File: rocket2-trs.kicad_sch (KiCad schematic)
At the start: 25 parts, among them J2 ARM Cortex Debug, J2 SMA, U4 AZ1117-3.3, Y1 16MHz

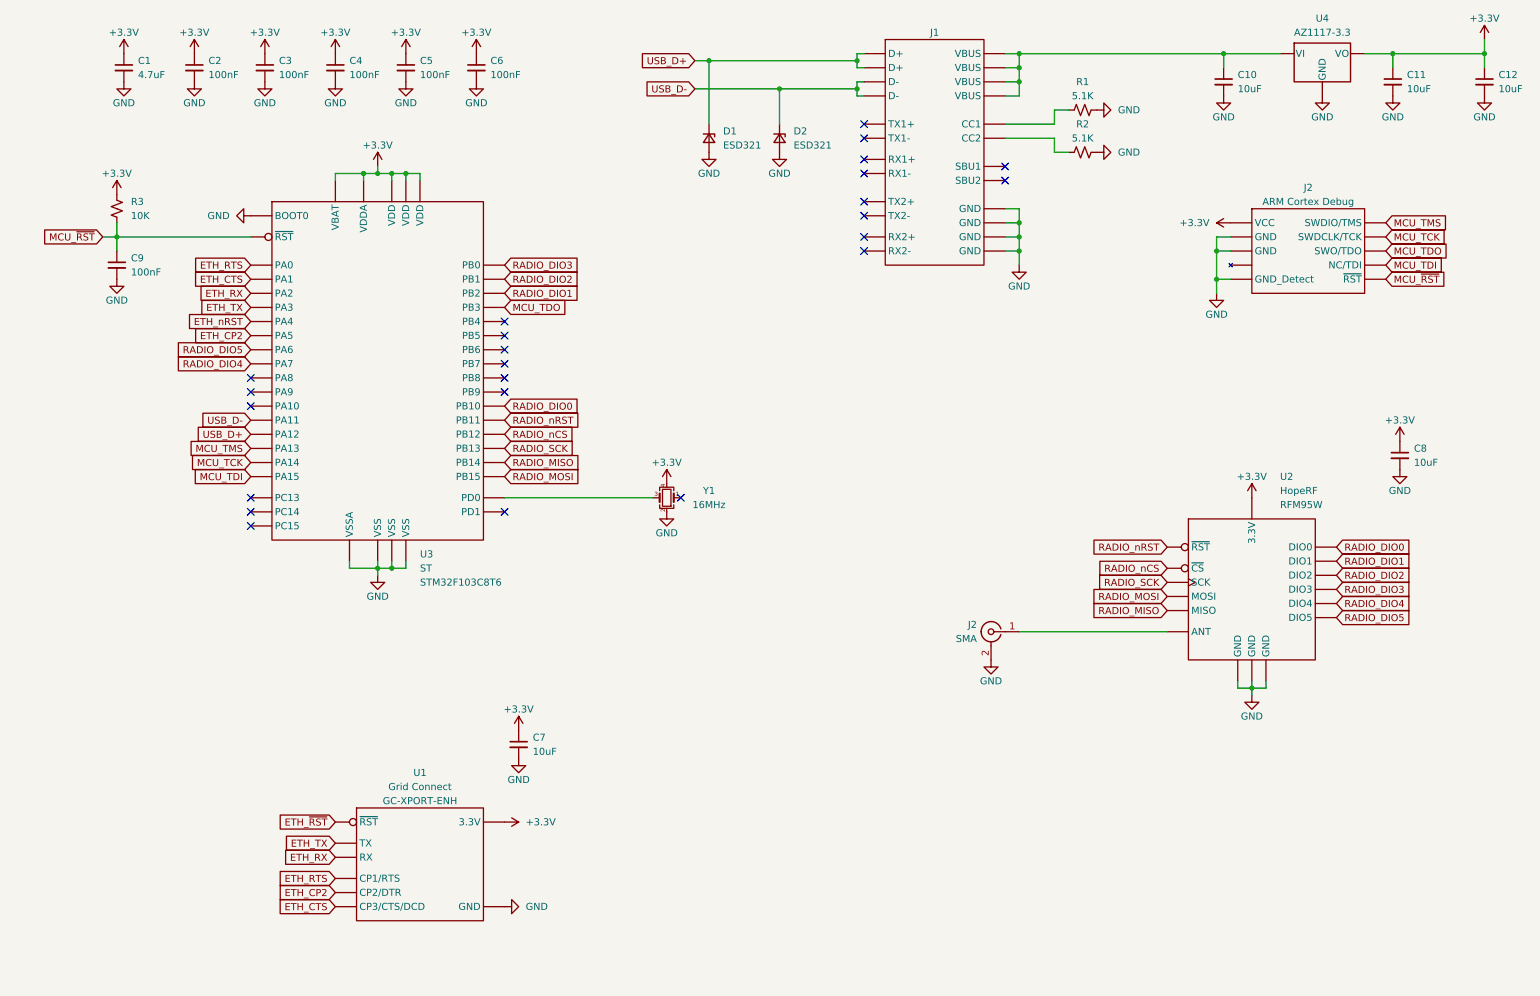
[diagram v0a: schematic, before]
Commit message: Add test points
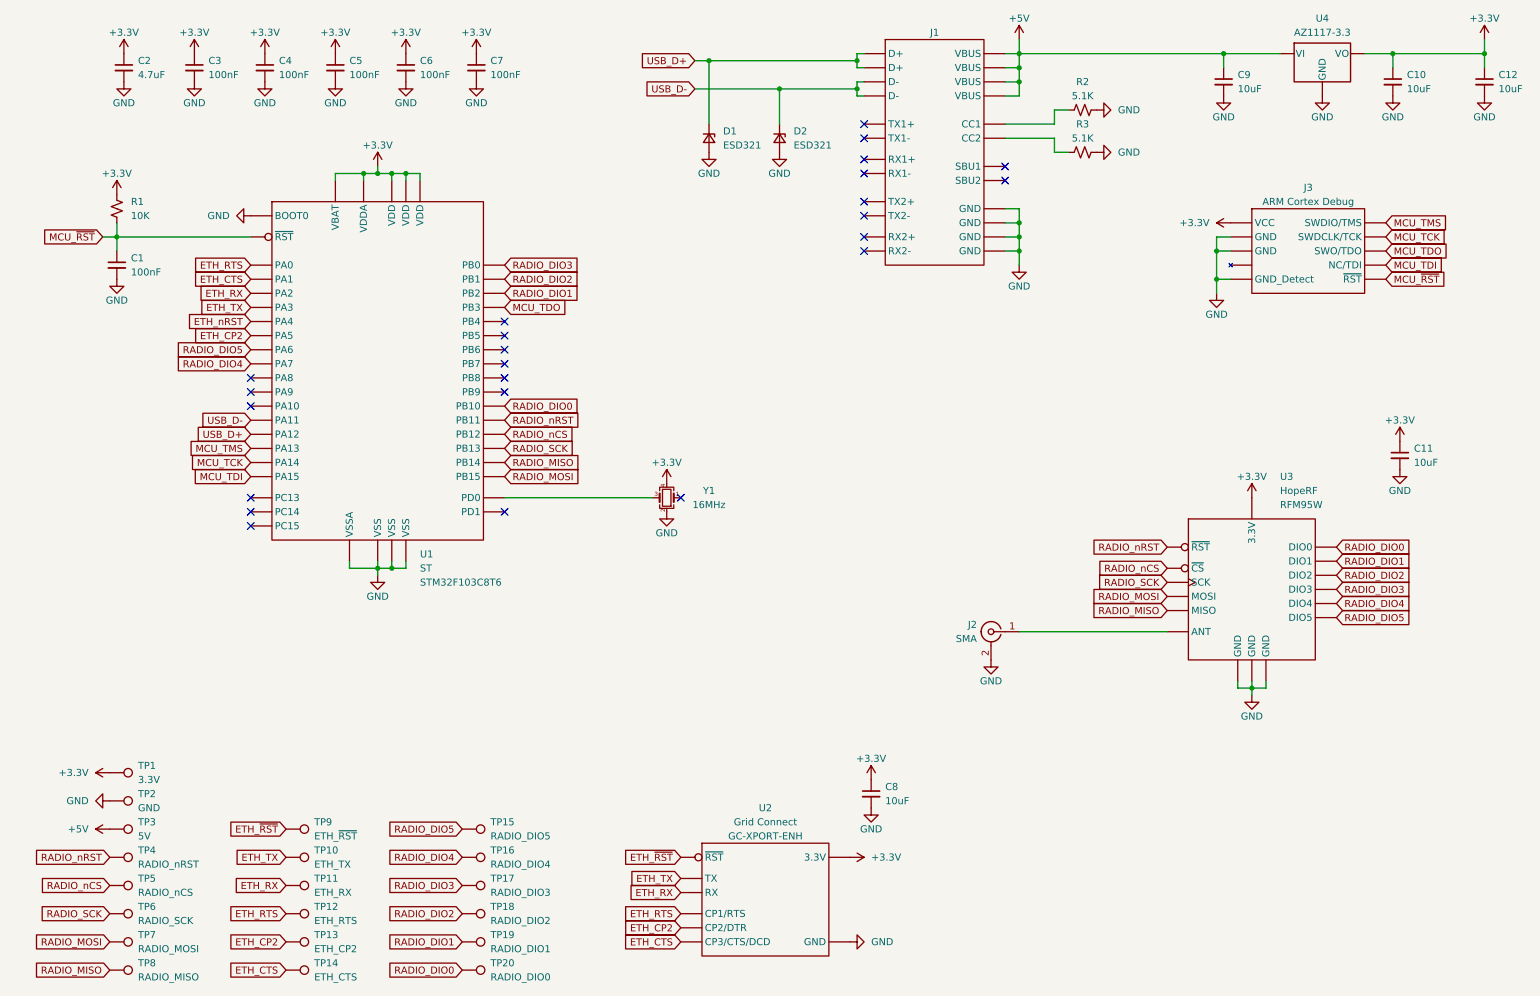
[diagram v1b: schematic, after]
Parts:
- added TP1: 3.3V, TestPoint:TestPoint_Pad_D1.0mm, symbol Connector:TestPoint
- added TP10: ETH_TX, TestPoint:TestPoint_Pad_D1.0mm, symbol Connector:TestPoint
- added TP11: ETH_RX, TestPoint:TestPoint_Pad_D1.0mm, symbol Connector:TestPoint
- added TP12: ETH_RTS, TestPoint:TestPoint_Pad_D1.0mm, symbol Connector:TestPoint
- added TP13: ETH_CP2, TestPoint:TestPoint_Pad_D1.0mm, symbol Connector:TestPoint
- added TP14: ETH_CTS, TestPoint:TestPoint_Pad_D1.0mm, symbol Connector:TestPoint
- added TP15: RADIO_DIO5, TestPoint:TestPoint_Pad_D1.0mm, symbol Connector:TestPoint
- added TP16: RADIO_DIO4, TestPoint:TestPoint_Pad_D1.0mm, symbol Connector:TestPoint
- added TP17: RADIO_DIO3, TestPoint:TestPoint_Pad_D1.0mm, symbol Connector:TestPoint
- added TP18: RADIO_DIO2, TestPoint:TestPoint_Pad_D1.0mm, symbol Connector:TestPoint
- added TP19: RADIO_DIO1, TestPoint:TestPoint_Pad_D1.0mm, symbol Connector:TestPoint
- added TP2: GND, TestPoint:TestPoint_Pad_D1.0mm, symbol Connector:TestPoint
- added TP20: RADIO_DIO0, TestPoint:TestPoint_Pad_D1.0mm, symbol Connector:TestPoint
- added TP3: 5V, TestPoint:TestPoint_Pad_D1.0mm, symbol Connector:TestPoint
- added TP4: RADIO_nRST, TestPoint:TestPoint_Pad_D1.0mm, symbol Connector:TestPoint
- added TP5: RADIO_nCS, TestPoint:TestPoint_Pad_D1.0mm, symbol Connector:TestPoint
- added TP6: RADIO_SCK, TestPoint:TestPoint_Pad_D1.0mm, symbol Connector:TestPoint
- added TP7: RADIO_MOSI, TestPoint:TestPoint_Pad_D1.0mm, symbol Connector:TestPoint
- added TP8: RADIO_MISO, TestPoint:TestPoint_Pad_D1.0mm, symbol Connector:TestPoint
- added TP9: ETH_~{RST}, TestPoint:TestPoint_Pad_D1.0mm, symbol Connector:TestPoint
- renumbered C9 to C1, C11 to C10, C8 to C11, C1 to C2, C2 to C3, C3 to C4, C4 to C5, C5 to C6, C6 to C7, C7 to C8, C10 to C9, J2 to J3, R3 to R1, R1 to R2, R2 to R3, U3 to U1, U1 to U2, U2 to U3
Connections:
- net +3.3V: now also TP1.1
- net ETH_CP2: now also TP13.1
- net ETH_CTS: now also TP14.1
- net ETH_RTS: now also TP12.1
- net ETH_RX: now also TP11.1
- net ETH_TX: now also TP10.1
- net ETH_~{RST}: now also TP9.1
- net GND: now also TP2.1
- net RADIO_DIO0: now also TP20.1
- net RADIO_DIO1: now also TP19.1
- net RADIO_DIO2: now also TP18.1
- net RADIO_DIO3: now also TP17.1
- net RADIO_DIO4: now also TP16.1
- net RADIO_DIO5: now also TP15.1
- net RADIO_MISO: now also TP8.1
- net RADIO_MOSI: now also TP7.1
- net RADIO_SCK: now also TP6.1
- net RADIO_nCS: now also TP5.1
- net RADIO_nRST: now also TP4.1
- net +5V: now reaches C9.1, J1.A4 (VBUS), J1.A9 (VBUS), J1.B4 (VBUS), J1.B9 (VBUS), U4.3 (VI)
- net +5V: now also TP3.1
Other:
- moved on the sheet: C8, U2

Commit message: Add PCB
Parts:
- TP9: value ETH_~{RST} -> ETH_nRST
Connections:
- net ETH_~{RST} is gone; now on net ETH_nRST: TP9.1, U2.3 (~{RST})
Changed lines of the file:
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@@
-    )
-  )
-  (global_label "ETH_~{RST}" (shape input) (at 130.81 171.45 180) (fields_autoplaced)
-    (effects (font (size 1.27 1.27)) (justify right))
-    (property "Intersheetrefs" "${INTERSHEET_REFS}" (at 119.963 171.45 0)
-      (effects (font (size 1.27 1.27)) (justify right) hide)
     )
   )
@@
     )
   )
+  (global_label "ETH_nRST" (shape input) (at 130.81 171.45 180) (fields_autoplaced)
+    (effects (font (size 1.27 1.27)) (justify right))
+    (property "Intersheetrefs" "${INTERSHEET_REFS}" (at 118.814 171.45 0)
+      (effects (font (size 1.27 1.27)) (justify right) hide)
+    )
+  )
   (global_label "ETH_CTS" (shape input) (at 130.81 186.69 180) (fields_autoplaced)
     (effects (font (size 1.27 1.27)) (justify right))
@@
     )
   )
+  (global_label "ETH_nRST" (shape input) (at 59.69 166.37 180) (fields_autoplaced)
+    (effects (font (size 1.27 1.27)) (justify right))
+    (property "Intersheetrefs" "${INTERSHEET_REFS}" (at 47.694 166.37 0)
+      (effects (font (size 1.27 1.27)) (justify right) hide)
+    )
+  )
   (global_label "MCU_~{RST}" (shape input) (at 26.67 59.69 180) (fields_autoplaced)
     (effects (font (size 1.27 1.27)) (justify right))
@@
     (effects (font (size 1.27 1.27)) (justify right))
     (property "Intersheetrefs" "${INTERSHEET_REFS}" (at 77.5879 176.53 0)
-      (effects (font (size 1.27 1.27)) (justify right) hide)
-    )
-  )
-  (global_label "ETH_~{RST}" (shape input) (at 59.69 166.37 180) (fields_autoplaced)
-    (effects (font (size 1.27 1.27)) (justify right))
-    (property "Intersheetrefs" "${INTERSHEET_REFS}" (at 48.9224 166.37 0)
       (effects (font (size 1.27 1.27)) (justify right) hide)
     )
@@
       (effects (font (size 1.27 1.27)) (justify left))
     )
-    (property "Value" "ETH_~{RST}" (at 64.77 167.64 90)
-      (effects (font (size 1.27 1.27)) (justify left))
-    )
+    (property "Value" "ETH_nRST" (at 64.77 167.64 90)
+      (effects (font (size 1.27 1.27)) (justify left))
+    )

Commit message: Add LED
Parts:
- added D3: LED, Diode_SMD:D_0603_1608Metric, symbol Device:LED_Small
- added R4: 1K, Resistor_SMD:R_0603_1608Metric, symbol Device:R_Small_US
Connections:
- net GND: now also D3.1 (K)
- net at U1.45 (PB8): now also R4.1
- new net: D3.2 (A), R4.2
- no-connect marks 24 -> 23
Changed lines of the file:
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@@
   (no_connect (at 53.34 106.68))
   (no_connect (at 53.34 90.17))
-  (no_connect (at 99.06 85.09))
   (no_connect (at 189.23 49.53))
   (no_connect (at 53.34 109.22))
@@
     (stroke (width 0) (type default))
   )
+  (wire (pts (xy 99.06 85.09) (xy 115.57 85.09))
+    (stroke (width 0) (type default))
+  )
   (wire (pts (xy 191.77 54.61) (xy 191.77 57.15))
     (stroke (width 0) (type default))
@@
     (stroke (width 0) (type default))
   )
+  (wire (pts (xy 120.65 85.09) (xy 127 85.09))
+    (stroke (width 0) (type default))
+  )
   (wire (pts (xy 135.89 27.94) (xy 135.89 39.37))
     (stroke (width 0) (type default))
@@
         (path "/f40df73a-33db-451b-892b-c732f49623c2"
           (reference "C7") (unit 1)
+        )
+      )
+    )
+  )
+  (symbol (lib_id "power:GND") (at 132.08 85.09 90) (unit 1)
+    (in_bom yes) (on_board yes) (dnp no) (fields_autoplaced)
+    (property "Reference" "#PWR045" (at 138.43 85.09 0)
+      (effects (font (size 1.27 1.27)) hide)
+    )
+    (property "Value" "GND" (at 135.89 85.09 90)
+      (effects (font (size 1.27 1.27)) (justify right))
+    )
+    (property "Footprint" "" (at 132.08 85.09 0)
+      (effects (font (size 1.27 1.27)) hide)
+    )
+    (property "Datasheet" "" (at 132.08 85.09 0)
+      (effects (font (size 1.27 1.27)) hide)
+    )
+    (pin "1")
+    (instances
+      (project "rocket2-trs"
+        (path "/f40df73a-33db-451b-892b-c732f49623c2"
+          (reference "#PWR045") (unit 1)
         )
       )
@@
         (path "/f40df73a-33db-451b-892b-c732f49623c2"
           (reference "#PWR044") (unit 1)
+        )
+      )
+    )
+  )
+  (symbol (lib_id "Device:LED_Small") (at 129.54 85.09 180) (unit 1)
+    (in_bom yes) (on_board yes) (dnp no)
+    (property "Reference" "D3" (at 129.54 80.01 0)
+      (effects (font (size 1.27 1.27)))
+    )
+    (property "Value" "LED" (at 129.54 82.55 0)
+      (effects (font (size 1.27 1.27)))
+    )
+    (property "Footprint" "Diode_SMD:D_0603_1608Metric" (at 129.54 85.09 90)
+      (effects (font (size 1.27 1.27)) hide)
+    )
+    (property "Datasheet" "~" (at 129.54 85.09 90)
+      (effects (font (size 1.27 1.27)) hide)
+    )
+    (property "Manufacturer" "Generic" (at 129.54 85.09 0)
+      (effects (font (size 1.27 1.27)) hide)
+    )
+    (property "Part #" "Generic 0603 Red LED" (at 129.54 85.09 0)
+      (effects (font (size 1.27 1.27)) hide)
+    )
+    (pin "2")
+    (pin "1")
+    (instances
+      (project "rocket2-trs"
+        (path "/f40df73a-33db-451b-892b-c732f49623c2"
+          (reference "D3") (unit 1)
         )
       )
@@
         )
       )
+    )
+  )
+  (symbol (lib_id "Device:R_Small_US") (at 118.11 85.09 90) (unit 1)
+    (in_bom yes) (on_board yes) (dnp no)
+    (property "Reference" "R4" (at 118.11 80.01 90)
+      (effects (font (size 1.27 1.27)))
+    )
+    (property "Value" "1K" (at 118.11 82.55 90)
+      (effects (font (size 1.27 1.27)))
+    )
+    (property "Footprint" "Resistor_SMD:R_0603_1608Metric" (at 118.11 85.09 0)
+      (effects (font (size 1.27 1.27)) hide)
+    )
+    (property "Datasheet" "~" (at 118.11 85.09 0)
+      (effects (font (size 1.27 1.27)) hide)
+    )
+    (property "Part #" "Generic 0603 1K 1% Resistor" (at 118.11 85.09 0)
+      (effects (font (size 1.27 1.27)) hide)
+    )
+    (property "Manufacturer" "Generic" (at 118.11 85.09 0)
+      (effects (font (size 1.27 1.27)) hide)
+    )
+    (pin "1")
+    (pin "2")
+    (instances
+      (project "rocket2-trs"
+        (path "/f40df73a-33db-451b-892b-c732f49623c2"
+          (reference "R4") (unit 1)
+        )
+      )

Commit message: TRS Update 1
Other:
- moved on the sheet: TP1, TP2

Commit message: add
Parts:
- added U5: LoRA-E5, UCIRP-KiCAD-Lib:LoRa - E5, symbol UCIRP-KiCAD-Lib:LoRa-E5

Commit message: bleh
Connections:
- net +3.3V: now also U5.2 (3V3)
- net ETH_RX: now also U5.20 (RX1_(PC0))
- net ETH_TX: now also U5.21 (TX1_(PC1))
- net GND: now also U5.12 (GND), U5.6 (GND)
- net RADIO_nRST: now also U5.5 (RST)
- net UART1 RX: now reaches U5.17 (RX_(PB7))
- net UART1 TX: now reaches U5.18 (TX_(PB6))

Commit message: trs update 12/14/2025
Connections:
- net +5V: now also U5.1 (5V)
- net UART1 RX: now also U1.31 (PA10)
- net UART1 TX: now also U1.30 (PA9)
- no-connect marks 23 -> 21

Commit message: TRS fixed
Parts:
- added J4, J5: Conn_01x12_MountingPin, symbol Connector_Generic_MountingPin:Conn_01x12_MountingPin
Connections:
- net +3.3V: now also J5.2 (Pin_2)
- net +5V: now also J5.1 (Pin_1)
- net ETH_CP2: now also U5.12 (GND), J5.12 (Pin_12)
- net ETH_CTS: now also U5.11 (DI0_(PB10)), J5.11 (Pin_11)
- net ETH_RX: now also J4.9 (Pin_9)
- net ETH_TX: now also J4.10 (Pin_10)
- net ETH_nRST: now also U5.19 (D0_(PA0)), J4.8 (Pin_8)
- net GND: now also J4.1 (Pin_1), J5.6 (Pin_6)
- net RADIO_nRST: no longer U5.5 (RST)
- net UART1 RX: now also J4.6 (Pin_6)
- net UART1 TX: now also J4.7 (Pin_7)
- new net LORA_RST: J5.5 (Pin_5), U5.5 (RST)
- no-connect marks 21 -> 47
